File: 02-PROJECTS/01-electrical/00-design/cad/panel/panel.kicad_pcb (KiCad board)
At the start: 2 copper layers, 200 x 70 mm, 50 parts, among them J1 panel ribbon 2x10 IDC, J2 illumination in, SW1 key - defog, SW10 encoder - fan, SW11 encoder - temperature, SW12 encoder - driver seat, SW13 encoder - passenger seat, SW2 key - hatch release, SW3 key - fuel-door release, SW4 key - HVAC mode, SW5 key - recirculate, SW6 key - window DRV up, SW7 key - window DRV down, SW8 key - window PASS up, SW9 key - window PASS down, U1 thumbstick - not chosen (P156)

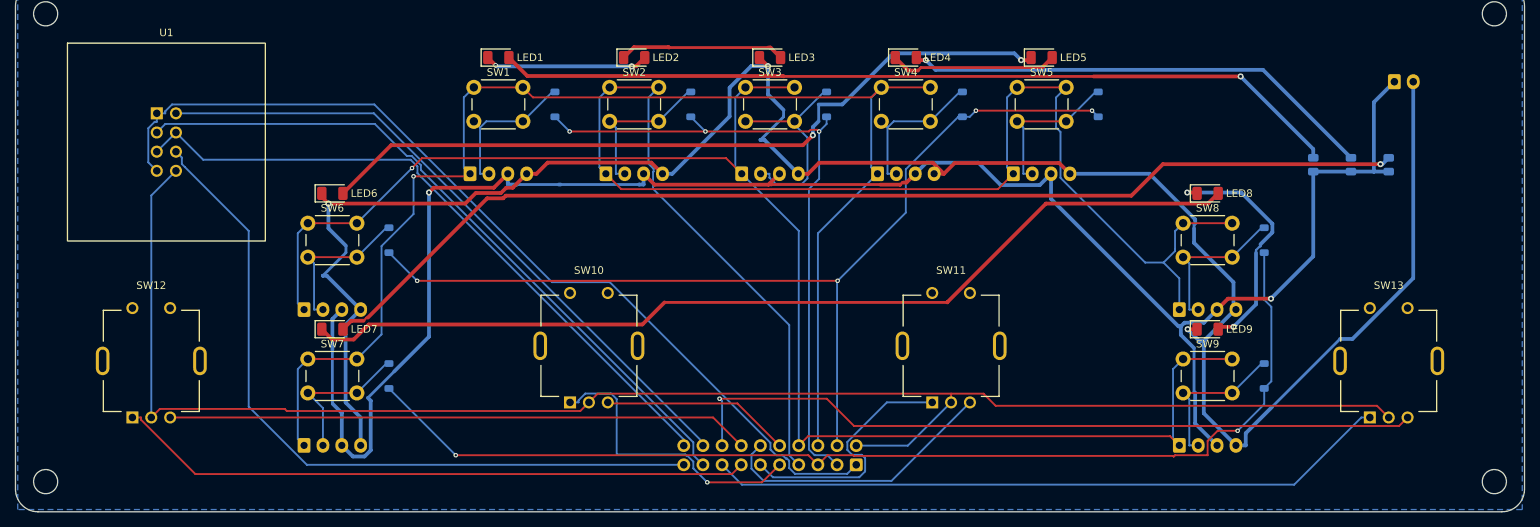
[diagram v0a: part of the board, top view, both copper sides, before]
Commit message: Electrical: the panel's lights and the 26-way ribbon, the panel as a board, the DCU's release pull-downs (D-458, D-459, D-465)
Panel rev 0.03: IS31FL3236A at 0x3C driving 9 key LEDs and 26 knob-arc LEDs, dimmed with the dash; J1 2 x 13; the faceplate windows table in its README; DRC 0/0/0, enclosure rebuilt. DCU sheet rev 0.04: J4 2 x 13, R71 / R72 series, F1 PTC on +5V_PNL, R39 / R41 10 k pull-downs; the board re-lay is Y12. panel_ribbon 21-26, P155 / P157 / P173-P175, P192 / P193, H-008, SN23; rows R-APPLY-01.14 / 01.15.

Co-Authored-By: Claude Fable 5.1 <noreply@anthropic.com>
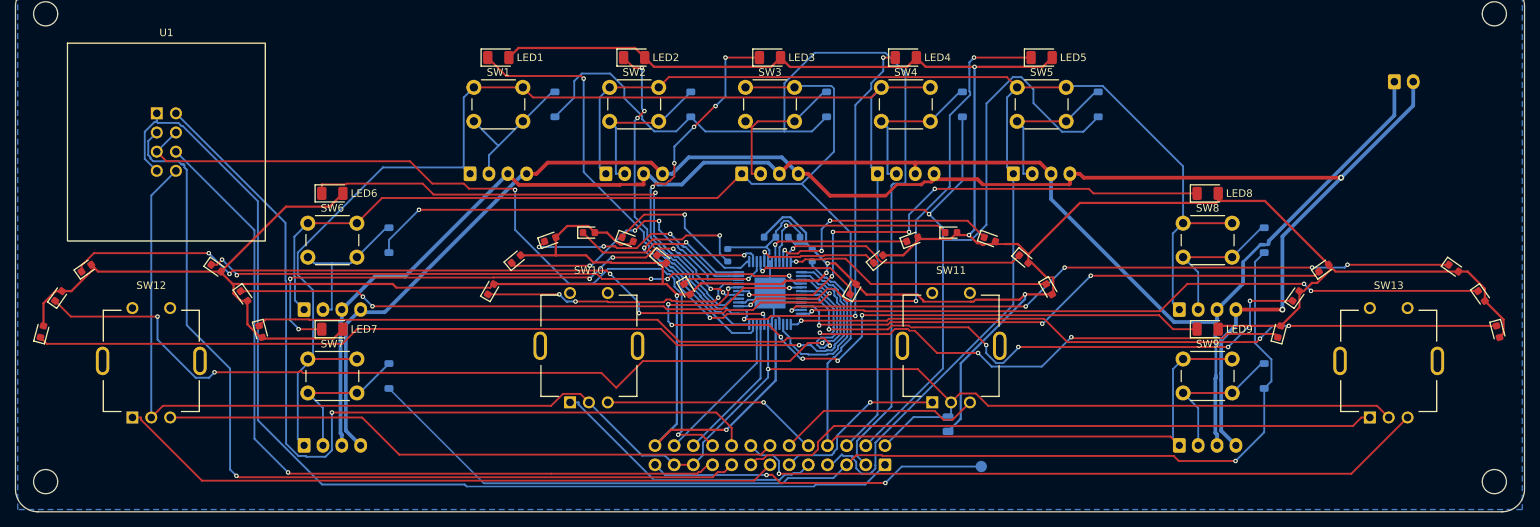
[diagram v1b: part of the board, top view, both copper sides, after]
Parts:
- removed R3: 1k - confirm, Resistor_SMD:R_0805_2012Metric
- added C1: 10u 16V X7R - confirm, Capacitor_SMD:C_0805_2012Metric, B.Cu at (173.6, 108.4)
- added C2: 1u, Capacitor_SMD:C_0603_1608Metric, B.Cu at (150.0, 83.6)
- added C3: 100n, Capacitor_SMD:C_0603_1608Metric, B.Cu at (153.2, 83.6)
- added LED10: fan level 1 - confirm, LED_SMD:LED_0603_1608Metric, F.Cu at (113.0, 90.5)
- added LED11: fan level 2 - confirm, LED_SMD:LED_0603_1608Metric, F.Cu at (116.4, 86.5)
- added LED12: fan level 3 - confirm, LED_SMD:LED_0603_1608Metric, F.Cu at (120.9, 83.9)
- added LED13: fan level 4 - confirm, LED_SMD:LED_0603_1608Metric, F.Cu at (126.0, 83.0)
- added LED14: fan level 5 - confirm, LED_SMD:LED_0603_1608Metric, F.Cu at (131.1, 83.9)
- added LED15: fan level 6 - confirm, LED_SMD:LED_0603_1608Metric, F.Cu at (135.6, 86.5)
- added LED16: fan level 7 - confirm, LED_SMD:LED_0603_1608Metric, F.Cu at (139.0, 90.5)
- added LED17: temperature level 1 - confirm, LED_SMD:LED_0603_1608Metric, F.Cu at (161.0, 90.5)
- added LED18: temperature level 2 - confirm, LED_SMD:LED_0603_1608Metric, F.Cu at (164.4, 86.5)
- added LED19: temperature level 3 - confirm, LED_SMD:LED_0603_1608Metric, F.Cu at (168.9, 83.9)
- added LED20: temperature level 4 - confirm, LED_SMD:LED_0603_1608Metric, F.Cu at (174.0, 83.0)
- added LED21: temperature level 5 - confirm, LED_SMD:LED_0603_1608Metric, F.Cu at (179.1, 83.9)
- added LED22: temperature level 6 - confirm, LED_SMD:LED_0603_1608Metric, F.Cu at (183.6, 86.5)
- added LED23: temperature level 7 - confirm, LED_SMD:LED_0603_1608Metric, F.Cu at (187.0, 90.5)
- added LED24: driver seat cool 3 - confirm, LED_SMD:LED_0603_1608Metric, F.Cu at (53.5, 96.1)
- added LED25: driver seat cool 2 - confirm, LED_SMD:LED_0603_1608Metric, F.Cu at (55.7, 91.4)
- added LED26: driver seat cool 1 - confirm, LED_SMD:LED_0603_1608Metric, F.Cu at (59.4, 87.7)
- added LED27: driver seat heat 1 - confirm, LED_SMD:LED_0603_1608Metric, F.Cu at (76.6, 87.7)
- added LED28: driver seat heat 2 - confirm, LED_SMD:LED_0603_1608Metric, F.Cu at (80.3, 91.4)
- added LED29: driver seat heat 3 - confirm, LED_SMD:LED_0603_1608Metric, F.Cu at (82.5, 96.1)
- added LED30: passenger seat cool 3 - confirm, LED_SMD:LED_0603_1608Metric, F.Cu at (217.5, 96.1)
- added LED31: passenger seat cool 2 - confirm, LED_SMD:LED_0603_1608Metric, F.Cu at (219.7, 91.4)
- added LED32: passenger seat cool 1 - confirm, LED_SMD:LED_0603_1608Metric, F.Cu at (223.4, 87.7)
- added LED33: passenger seat heat 1 - confirm, LED_SMD:LED_0603_1608Metric, F.Cu at (240.6, 87.7)
- added LED34: passenger seat heat 2 - confirm, LED_SMD:LED_0603_1608Metric, F.Cu at (244.3, 91.4)
- added LED35: passenger seat heat 3 - confirm, LED_SMD:LED_0603_1608Metric, F.Cu at (246.5, 96.1)
- added TP1: ribbon spare, TestPoint:TestPoint_Pad_D1.5mm, B.Cu at (178.0, 114.0)
- added U2: IS31FL3236A-TQLS4, Package_QFP:TQFP-48-1EP_7x7mm_P0.5mm_EP4.11x4.11mm, B.Cu at (150.0, 91.0)
- J1: value panel ribbon 2x10 IDC -> panel ribbon 2x13 IDC, keyed; footprint Connector_IDC:IDC-Header_2x10_P2.54mm_Vertical -> Connector_IDC:IDC-Header_2x13_P2.54mm_Vertical
- LED1: value backlight defog - confirm -> key light defog - confirm
- LED2: value backlight hatch release - confirm -> key light hatch release - confirm
- LED3: value backlight fuel-door release - confirm -> key light fuel-door release - confirm
- LED4: value backlight HVAC mode - confirm -> key light HVAC mode - confirm
- LED5: value backlight recirculate - confirm -> key light recirculate - confirm
- LED6: value backlight window DRV up - confirm -> key light window DRV up - confirm
- LED7: value backlight window DRV down - confirm -> key light window DRV down - confirm
- LED8: value backlight window PASS up - confirm -> key light window PASS up - confirm
- LED9: value backlight window PASS down - confirm -> key light window PASS down - confirm
- R1: value 1k - confirm -> 10k; footprint Resistor_SMD:R_0805_2012Metric -> Resistor_SMD:R_0603_1608Metric
- R2: value 1k - confirm -> 100k; footprint Resistor_SMD:R_0805_2012Metric -> Resistor_SMD:R_0603_1608Metric
- moved R1 78.5 mm to (144.4, 86.0)
- moved R2 72.4 mm to (155.6, 86.0)
- moved J1 3.81 mm to (165.2, 113.8)
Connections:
- LED1 pad 1: /BL1_2 -> /LK1
- LED1 pad 2: /BL1_1 -> /+5V_PNL
- LED2 pad 1: /BL1_3 -> /LK2
- LED2 pad 2: /BL1_2 -> /+5V_PNL
- LED3 pad 1: /ILLUM_GND -> /LK3
- LED3 pad 2: /BL1_3 -> /+5V_PNL
- LED4 pad 1: /BL2_2 -> /LK4
- LED4 pad 2: /BL2_1 -> /+5V_PNL
- LED5 pad 1: /BL2_3 -> /LK5
- LED5 pad 2: /BL2_2 -> /+5V_PNL
- LED6 pad 1: /ILLUM_GND -> /LK6
- LED6 pad 2: /BL2_3 -> /+5V_PNL
- LED7 pad 1: /BL3_2 -> /LK7
- LED7 pad 2: /BL3_1 -> /+5V_PNL
- LED8 pad 1: /BL3_3 -> /LK8
- LED8 pad 2: /BL3_2 -> /+5V_PNL
- LED9 pad 1: /ILLUM_GND -> /LK9
- LED9 pad 2: /BL3_3 -> /+5V_PNL
- R1 pad 1: /ILLUM_12V -> /LED_REXT
- R1 pad 2: /BL1_1 -> GND
- R2 pad 1: /ILLUM_12V -> /LED_SDB
- R2 pad 2: /BL2_1 -> /+5V_PNL
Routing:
- net /+5V_PNL: track 0.00 -> 536.1 mm, vias 0 -> 7
- net /BL3_1: track 148.0 -> 0.00 mm, vias 1 -> 0
- net /BL3_2: track 127.4 -> 0.00 mm
- net /LSD2: track 0.00 -> 125.5 mm, vias 0 -> 3
- net /LSD1: track 0.00 -> 122.2 mm, vias 0 -> 1
- net /BL1_1: track 112.8 -> 0.00 mm, vias 1 -> 0
- net /LSD3: track 0.00 -> 110.7 mm, vias 0 -> 5
- net /BL2_3: track 101.3 -> 0.00 mm, vias 2 -> 0
- net /LSP6: track 0.00 -> 96.0 mm, vias 0 -> 3
- net /LSD6: track 0.00 -> 92.6 mm, vias 0 -> 1
- net /LSP5: track 0.00 -> 91.8 mm, vias 0 -> 3
- net /LSP4: track 0.00 -> 90.9 mm, vias 0 -> 5
- net /LK9: track 0.00 -> 90.5 mm, vias 0 -> 7
- net /LSD4: track 0.00 -> 80.7 mm, vias 0 -> 5
- net /LSP2: track 0.00 -> 76.7 mm, vias 0 -> 5
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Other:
- board text added: "OFF"
- board text added: "PROVISIONAL (Y6, D-455)"
- board text added: "RX-7 control panel rev 0.03"
- board text added: "faceplate side (F): keys, knobs, thumbstick, 35 LED windows (README); back (B): ribbon J1 2x13, diodes, light driver U2, (b) leads"
- board text added: "key style: luxury 03.14"
- board text added: "keys SW1-9 (a) fitted, SWB1-9 (b) DNP"
- board text added: "lights D-458: U2 IS31FL3236A at 0x3C"
- board text added: "outline 200 x 70, holes: confirm (V-113)"
- board text removed: "RX-7 control panel - PROVISIONAL (Y6, D-455)"
- board text removed: "faceplate side (F): keys, knobs, thumbstick in the 0x400 key order; back (B): ribbon J1, diodes, illumination, (b) leads"
- board text removed: "keys: SW1-9 style (a) fitted / SWB1-9 style (b) DNP - luxury 03.14"
- board text removed: "outline 200 x 70 mm and holes: confirm - V-113 measures the dash opening"

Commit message: Electrical: the panel board redrawn to the ruled control set and the DCU sheet renamed to the ribbon; both packaged for the bench order with the upper board (Y20)
panel rev 0.04: 180 x 84.76 mm with the controls where the sketch puts them, a 4 x 3 matrix, one centre encoder with push, two seat encoders, DPDT sprung window switches, the screen header behind its window with a supply jumper, the LED driver with 24 LEDs, the 26-way ribbon and the 2 x 6 plate header; ERC 0, DRC and parity 0, check.py 79 checks 0 mismatches. The DCU carrier's ribbon nets renamed (sheet, symbol pins, board net names only; DRC and parity 0, check.py 163 / 0); check.py's panel and dcu entries follow the record. Found and recorded: the window switches must be double-pole, the screen a 3.3 V-bus module, the seat symbol cannot sit in the knob's centre without a hollow-shaft encoder. Gerbers, drills and BOMs for the panel and upper boards under fab/ for Y18; the climate-unit mock-up's ribbon header at the drawn 16.5 mm, rebuilt clear.

Co-Authored-By: Claude Fable 5.1 <noreply@anthropic.com>
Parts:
- removed D9: 1N4148W, Diode_SMD:D_SOD-123
- removed LED25: driver seat cool 2 - confirm, LED_SMD:LED_0603_1608Metric
- removed LED26: driver seat cool 1 - confirm, LED_SMD:LED_0603_1608Metric
- removed LED27: driver seat heat 1 - confirm, LED_SMD:LED_0603_1608Metric
- removed LED28: driver seat heat 2 - confirm, LED_SMD:LED_0603_1608Metric
- removed LED29: driver seat heat 3 - confirm, LED_SMD:LED_0603_1608Metric
- removed LED30: passenger seat cool 3 - confirm, LED_SMD:LED_0603_1608Metric
- removed LED31: passenger seat cool 2 - confirm, LED_SMD:LED_0603_1608Metric
- removed LED32: passenger seat cool 1 - confirm, LED_SMD:LED_0603_1608Metric
- removed LED33: passenger seat heat 1 - confirm, LED_SMD:LED_0603_1608Metric
- removed LED34: passenger seat heat 2 - confirm, LED_SMD:LED_0603_1608Metric
- removed LED35: passenger seat heat 3 - confirm, LED_SMD:LED_0603_1608Metric
- removed SW10: encoder - fan, panel:RotaryEncoder_Bourns_Vertical_PEC11R-4xxxF-Sxxxx
- removed SW11: encoder - temperature, panel:RotaryEncoder_Bourns_Vertical_PEC11R-4xxxF-Sxxxx
- removed SW12: encoder - driver seat, panel:RotaryEncoder_Bourns_Vertical_PEC11R-4xxxF-Sxxxx
- removed SW13: encoder - passenger seat, panel:RotaryEncoder_Bourns_Vertical_PEC11R-4xxxF-Sxxxx
- removed SWB1: key (b) - defog, Connector_JST:JST_XH_B4B-XH-A_1x04_P2.50mm_Vertical
- removed SWB2: key (b) - hatch release, Connector_JST:JST_XH_B4B-XH-A_1x04_P2.50mm_Vertical
- removed SWB3: key (b) - fuel-door release, Connector_JST:JST_XH_B4B-XH-A_1x04_P2.50mm_Vertical
- removed SWB4: key (b) - HVAC mode, Connector_JST:JST_XH_B4B-XH-A_1x04_P2.50mm_Vertical
- removed SWB5: key (b) - recirculate, Connector_JST:JST_XH_B4B-XH-A_1x04_P2.50mm_Vertical
- removed SWB6: key (b) - window DRV up, Connector_JST:JST_XH_B4B-XH-A_1x04_P2.50mm_Vertical
- removed SWB7: key (b) - window DRV down, Connector_JST:JST_XH_B4B-XH-A_1x04_P2.50mm_Vertical
- removed SWB8: key (b) - window PASS up, Connector_JST:JST_XH_B4B-XH-A_1x04_P2.50mm_Vertical
- removed SWB9: key (b) - window PASS down, Connector_JST:JST_XH_B4B-XH-A_1x04_P2.50mm_Vertical
- removed U1: thumbstick - not chosen (P156), panel:Thumbstick_P156_Placeholder_2x04_P2.54mm
- added J3: plate header 2x6 IDC, keyed (DP-DCU-E 1-12), Connector_IDC:IDC-Header_2x06_P2.54mm_Vertical, B.Cu at (156.3, 79.9)
- added JP1: screen supply 1-2 +5V_PNL / 2-3 +3V3, Jumper:SolderJumper-3_P1.3mm_Open_RoundedPad1.0x1.5mm, B.Cu at (101.0, 12.0)
- C1: value 10u 16V X7R - confirm -> 10uF 16V X7R
- C2: value 1u -> 1uF
- C3: value 100n -> 100nF
- H1, H2, H3, H4: value M3 - confirm against V-113 / LP20 -> M3
- J2: value illumination in -> screen module I2C 4-pin; footprint Connector_JST:JST_XH_B2B-XH-A_1x02_P2.50mm_Vertical -> Connector_PinHeader_2.54mm:PinHeader_1x04_P2.54mm_Vertical; moved to F.Cu
- LED1: value key light defog - confirm -> key light rear defog; footprint LED_SMD:LED_1206_3216Metric -> LED_SMD:LED_0603_1608Metric
- LED10: value fan level 1 - confirm -> window symbol PASS
- LED11: value fan level 2 - confirm -> seat symbol DRV
- LED12: value fan level 3 - confirm -> seat symbol PASS
- LED13: value fan level 4 - confirm -> driver seat cool 3
- LED14: value fan level 5 - confirm -> driver seat cool 2
- LED15: value fan level 6 - confirm -> driver seat cool 1
- LED16: value fan level 7 - confirm -> driver seat heat 1
- LED17: value temperature level 1 - confirm -> driver seat heat 2
- LED18: value temperature level 2 - confirm -> driver seat heat 3
- LED19: value temperature level 3 - confirm -> passenger seat cool 3
- LED2: value key light hatch release - confirm -> key light HVAC mode; footprint LED_SMD:LED_1206_3216Metric -> LED_SMD:LED_0603_1608Metric
- LED20: value temperature level 4 - confirm -> passenger seat cool 2
- LED21: value temperature level 5 - confirm -> passenger seat cool 1
- LED22: value temperature level 6 - confirm -> passenger seat heat 1
- LED23: value temperature level 7 - confirm -> passenger seat heat 2
- LED24: value driver seat cool 3 - confirm -> passenger seat heat 3
- LED3: value key light fuel-door release - confirm -> key light recirculate; footprint LED_SMD:LED_1206_3216Metric -> LED_SMD:LED_0603_1608Metric
- LED4: value key light HVAC mode - confirm -> key light mirror defog; footprint LED_SMD:LED_1206_3216Metric -> LED_SMD:LED_0603_1608Metric
- LED5: value key light recirculate - confirm -> knob ring 1; footprint LED_SMD:LED_1206_3216Metric -> LED_SMD:LED_0603_1608Metric
- LED6: value key light window DRV up - confirm -> knob ring 2; footprint LED_SMD:LED_1206_3216Metric -> LED_SMD:LED_0603_1608Metric
- LED7: value key light window DRV down - confirm -> knob ring 3; footprint LED_SMD:LED_1206_3216Metric -> LED_SMD:LED_0603_1608Metric
- LED8: value key light window PASS up - confirm -> knob ring 4; footprint LED_SMD:LED_1206_3216Metric -> LED_SMD:LED_0603_1608Metric
- LED9: value key light window PASS down - confirm -> window symbol DRV; footprint LED_SMD:LED_1206_3216Metric -> LED_SMD:LED_0603_1608Metric
- SW1: value key - defog -> key - rear defog
- SW2: value key - hatch release -> key - HVAC mode
- SW3: value key - fuel-door release -> key - recirculate
- SW4: value key - HVAC mode -> key - mirror defog
- SW5: value key - recirculate -> window DRV; footprint Button_Switch_THT:SW_PUSH_6mm_H13mm -> panel:Toggle_DPDT_SubMini_2x3_P2.54mm
- SW6: value key - window DRV up -> window PASS; footprint Button_Switch_THT:SW_PUSH_6mm_H13mm -> panel:Toggle_DPDT_SubMini_2x3_P2.54mm
- SW7: value key - window DRV down -> encoder - centre; footprint Button_Switch_THT:SW_PUSH_6mm_H13mm -> panel:RotaryEncoder_Bourns_Vertical_PEC11R-4xxxF-Sxxxx
- SW8: value key - window PASS up -> encoder - driver seat; footprint Button_Switch_THT:SW_PUSH_6mm_H13mm -> panel:RotaryEncoder_Bourns_Vertical_PEC11R-4xxxF-Sxxxx
- SW9: value key - window PASS down -> encoder - passenger seat; footprint Button_Switch_THT:SW_PUSH_6mm_H13mm -> panel:RotaryEncoder_Bourns_Vertical_PEC11R-4xxxF-Sxxxx
- moved LED9 205.8 mm to (12.0, 33.0)
- moved D5 173.7 mm to (21.0, 45.4)
- moved SW5 172.1 mm to (12.0, 42.4)
- moved SW8 169.4 mm to (40.0, 42.4)
- moved D4 156.8 mm to (21.0, 39.4)
- moved J2 155.2 mm to (86.2, 12.0), turned to 90 degrees
- moved LED8 128.3 mm to (80.5, 63.9)
- moved LED15 119.5 mm to (29.4, 31.8), turned to 0 degrees
- moved LED17 119.4 mm to (54.1, 37.2), turned to 0 degrees
- moved LED18 117.5 mm to (54.9, 43.7), turned to 0 degrees
- moved LED14 115.1 mm to (25.9, 37.2), turned to 0 degrees
- moved LED24 114.2 mm to (154.9, 43.7), turned to 0 degrees
- moved LED13 108.3 mm to (25.1, 43.7)
- moved LED5 106.6 mm to (80.5, 44.8)
- moved LED16 106.1 mm to (50.6, 31.8), turned to 0 degrees
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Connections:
- net /K6_23 renamed Net-(D6-A)
- D1 pad 2: /K1_11 -> Net-(D1-A)
- D2 pad 1: /ROW1 -> /ROW2
- D2 pad 2: /K2_12 -> Net-(D2-A)
- D3 pad 1: /ROW1 -> /ROW2
- D3 pad 2: /K3_13 -> Net-(D3-A)
- D4 pad 2: /K4_21 -> Net-(D4-A)
- D5 pad 1: /ROW2 -> /ROW3
- D5 pad 2: /K5_22 -> Net-(D5-A)
- D6 pad 1: /ROW2 -> /ROW3
- D7 pad 2: /K7_31 -> Net-(D7-A)
- D8 pad 1: /ROW3 -> /ROW4
- D8 pad 2: /K8_32 -> Net-(D8-A)
- J1 pad 10: /ENC_FAN_B -> /ENC_CENTRE_B
- J1 pad 11: /ENC_TEMP_A -> /ENC_CENTRE_PUSH
- J1 pad 12: /ENC_TEMP_B -> /ROW4
- J1 pad 9: /ENC_FAN_A -> /ENC_CENTRE_A
- J2 pad 1: /ILLUM_12V -> GND
- J2 pad 2: /ILLUM_GND -> /SCR_VCC
- LED10 pad 1: /LF1 -> /LW2
- LED11 pad 1: /LF2 -> /LS1
- LED12 pad 1: /LF3 -> /LS2
- LED13 pad 1: /LF4 -> /LSD1
- LED14 pad 1: /LF5 -> /LSD2
- LED15 pad 1: /LF6 -> /LSD3
- LED16 pad 1: /LF7 -> /LSD4
- LED17 pad 1: /LT1 -> /LSD5
- LED18 pad 1: /LT2 -> /LSD6
- LED19 pad 1: /LT3 -> /LSP1
- LED20 pad 1: /LT4 -> /LSP2
- LED21 pad 1: /LT5 -> /LSP3
- LED22 pad 1: /LT6 -> /LSP4
- LED23 pad 1: /LT7 -> /LSP5
- LED24 pad 1: /LSD1 -> /LSP6
- LED5 pad 1: /LK5 -> /LR1
- LED6 pad 1: /LK6 -> /LR2
- LED7 pad 1: /LK7 -> /LR3
- LED8 pad 1: /LK8 -> /LR4
- LED9 pad 1: /LK9 -> /LW1
- R2 pad 1: /LED_SDB -> /+5V_PNL
- R2 pad 2: /+5V_PNL -> /LED_SDB
- SW1 pad 1: /COL1 -> Net-(D1-A)
- SW1 pad 2: /K1_11 -> /COL1
- SW2 pad 1: /COL2 -> Net-(D2-A)
- SW2 pad 2: /K2_12 -> /COL1
- SW3 pad 1: /COL3 -> Net-(D3-A)
- SW3 pad 2: /K3_13 -> /COL2
- SW4 pad 1: /COL1 -> Net-(D8-A)
- SW4 pad 2: /K4_21 -> /COL1
- SW5 pad 1: /COL2 -> unconnected-(SW5-DN_1-Pad1)
- SW5 pad 2: /K5_22 -> Net-(D4-A)
- SW6 pad 1: /COL3 -> unconnected-(SW6-DN_1-Pad1)
- SW7 pad 1: /COL1 -> /ENC_CENTRE_A
- SW7 pad 2: /K7_31 -> GND
- SW8 pad 1: /COL2 -> /ENC_SEAT_DRV_A
- SW8 pad 2: /K8_32 -> GND
- SW9 pad 1: /COL3 -> /ENC_SEAT_PASS_A
- SW9 pad 2: /K9_33 -> GND
- U2 pad 1: /LK3 -> /LR4
- U2 pad 10: /LF2 -> /LSD5
- U2 pad 11: /LF3 -> unconnected-(U2-OUT12-Pad11)
- U2 pad 12: /LF4 -> /LSD2
- U2 pad 13: /LF5 -> /LSD4
- U2 pad 14: /LF6 -> /LW1
- U2 pad 15: /LF7 -> unconnected-(U2-OUT16-Pad15)
- U2 pad 16: /LT1 -> /LSD3
- U2 pad 17: /LT2 -> /LS1
- U2 pad 2: /LK4 -> unconnected-(U2-OUT4-Pad2)
- U2 pad 20: /LT3 -> /LS2
- U2 pad 21: /LT4 -> unconnected-(U2-OUT20-Pad21)
- U2 pad 22: /LT5 -> /LSP4
- U2 pad 23: /LT6 -> /LW2
- U2 pad 24: /LT7 -> /LSP3
- U2 pad 25: /LSD1 -> unconnected-(U2-OUT24-Pad25)
- U2 pad 26: /LSD2 -> /LSP5
- U2 pad 27: /LSD3 -> /LSP2
- U2 pad 28: /LSD4 -> /LSP6
- U2 pad 29: /LSD5 -> unconnected-(U2-OUT28-Pad29)
- U2 pad 3: /LK5 -> /LK1
- U2 pad 30: /LSD6 -> /LSP1
- U2 pad 31: /LSP1 -> /LK3
- U2 pad 32: /LSP2 -> /LR2
- U2 pad 34: /LSP3 -> unconnected-(U2-OUT32-Pad34)
- U2 pad 35: /LSP4 -> /LK4
- U2 pad 36: /LSP5 -> /LR3
- U2 pad 37: /LSP6 -> unconnected-(U2-OUT35-Pad37)
- U2 pad 47: /LK1 -> unconnected-(U2-OUT1-Pad47)
- U2 pad 48: /LK2 -> unconnected-(U2-OUT2-Pad48)
- U2 pad 5: /LK6 -> /LR1
- U2 pad 6: /LK7 -> /LK2
- U2 pad 7: /LK8 -> unconnected-(U2-OUT8-Pad7)
- U2 pad 8: /LK9 -> /LSD6
- U2 pad 9: /LF1 -> /LSD1
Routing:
- net /ILLUM_GND: track 228.2 -> 0.00 mm, vias 2 -> 0
- net /ILLUM_12V: track 217.4 -> 0.00 mm
- net /+5V_PNL: track 536.1 -> 320.6 mm, vias 7 -> 10
- net /JOY_X: track 119.3 -> 6.96 mm, vias 1 -> 0
- net /JOY_Y: track 118.2 -> 12.5 mm
- net /AGND: track 110.3 -> 9.88 mm, vias 2 -> 1
- net /JOY_PRESS: track 105.5 -> 6.92 mm, vias 1 -> 0
- net /PNL_SDA: track 19.8 -> 114.6 mm, vias 0 -> 8
- net /COL2: track 188.3 -> 94.5 mm, vias 0 -> 2
- net /PNL_SCL: track 20.6 -> 111.7 mm, vias 0 -> 3
- net /LK9: track 90.5 -> 0.00 mm, vias 7 -> 0
- net /LW1: track 0.00 -> 85.1 mm, vias 0 -> 1
- net /ENC_CENTRE_A: track 0.00 -> 84.4 mm, vias 0 -> 3
- net /ENC_CENTRE_PUSH: track 0.00 -> 82.9 mm, vias 0 -> 2
- net /LW2: track 0.00 -> 80.1 mm, vias 0 -> 3
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- added copper zone on F.Cu, net GND
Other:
- board size 200 x 70 mm -> 180 x 84.8 mm
- board text added: "Board 180 x 84.76 = the face less 6 a side (climate-unit PANEL_MARGIN) - confirm until V-113"
- board text added: "Cmts.User: the faceplate's cut-outs, the sketch's 180 x 60 block (panel-concept.html, D-492) centred on the 192 x 96.76 face"
- board text added: "J1 RIBBON TO DCU J4"
- board text added: "J3 LEFT PLATE (DP-DCU-E)"
- board text added: "Rx7 control panel rev 0.04 Y20 (D-492)"
- board text added: "centre knob 20"
- board text added: "driver seat 22"
- board text added: "fan mode"
- board text added: "mirror defog"
- board text added: "passenger seat 22"
- board text added: "provisional - outline confirm (V-113)"
- board text added: "rear defog"
- board text added: "recirculate"
- board text added: "screen window 44 x 23.6 (P201)"
- board text added: "window DRV"
- board text added: "window PASS"
- board text removed: "DEFOG"
- board text removed: "DRV DN"
- board text removed: "DRV SEAT"
- board text removed: "DRV UP"
- board text removed: "FAN"
- board text removed: "FUEL"
- board text removed: "HATCH"
- board text removed: "MIRROR"
- board text removed: "MODE"
- board text removed: "OFF"
- board text removed: "PASS DN"
- board text removed: "PASS SEAT"
- board text removed: "PASS UP"
- board text removed: "PROVISIONAL (Y6, D-455)"
- board text removed: "PROVISIONAL OUTLINE - confirm (V-113, D-455): 200 x 70 mm, R3 corners, M3 holes 4 mm in"
- board text removed: "RECIRC"
- board text removed: "RX-7 control panel rev 0.03"
- board text removed: "TEMP"
- board text removed: "faceplate side (F): keys, knobs, thumbstick, 35 LED windows (README); back (B): ribbon J1 2x13, diodes, light driver U2, (b) leads"
- board text removed: "key style: luxury 03.14"
- board text removed: "keys SW1-9 (a) fitted, SWB1-9 (b) DNP"
- board text removed: "lights D-458: U2 IS31FL3236A at 0x3C"
- board text removed: "outline 200 x 70, holes: confirm (V-113)"
